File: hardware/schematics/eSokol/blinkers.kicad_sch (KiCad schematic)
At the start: 21 parts, among them Q5 AO3400A, Q8 AO3400A, SW6 SW_SPDT_MSM, U6 NE555D

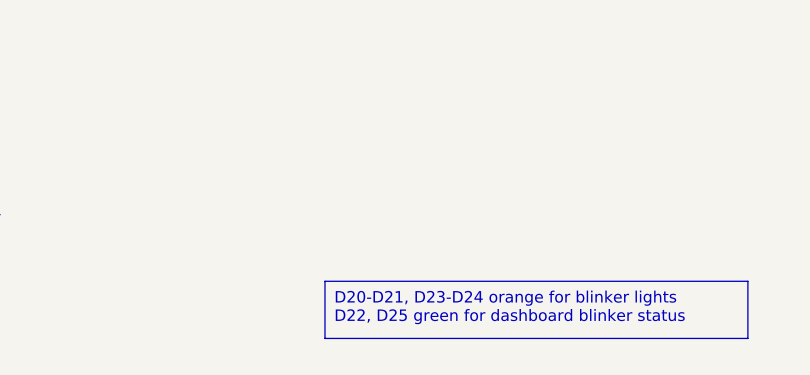
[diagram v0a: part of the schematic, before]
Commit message: hardware/schematics: finish-ify blinkers circuit, mark old blinkers circuit as outdated
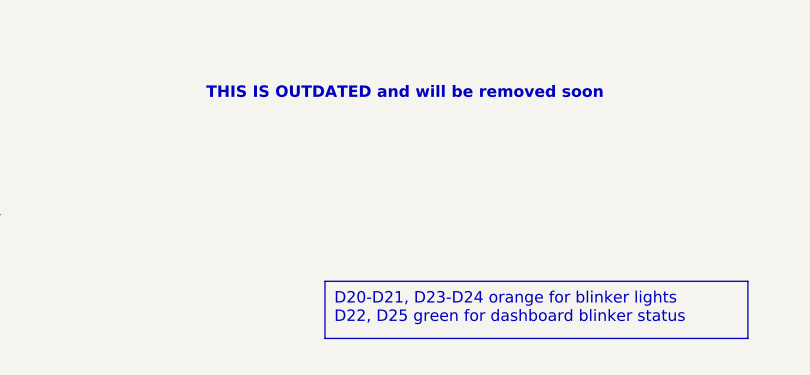
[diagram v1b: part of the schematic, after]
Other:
- note added: "THIS IS OUTDATED and will be removed soon"
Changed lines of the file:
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@@
+		)
+	)
+	(text "THIS IS OUTDATED and will be removed soon"
+		(exclude_from_sim no)
+		(at 223.52 73.152 0)
+		(effects
+			(font
+				(size 1.27 1.27)
+				(thickness 0.254)
+				(bold yes)
+			)
 		)
 	)
